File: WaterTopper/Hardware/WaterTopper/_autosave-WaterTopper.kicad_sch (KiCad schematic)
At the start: 61 parts, among them J1 TYPE-C-31-M-12, J2 Barrel_Jack_Switch, J3 Conn_01x07, J4 Conn_01x04, J5 Conn_01x04, J6 Conn_01x04, J7 Conn_01x04, J8 Screw_Terminal_01x02, J9 Screw_Terminal_01x02, SW1 SW_SPST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

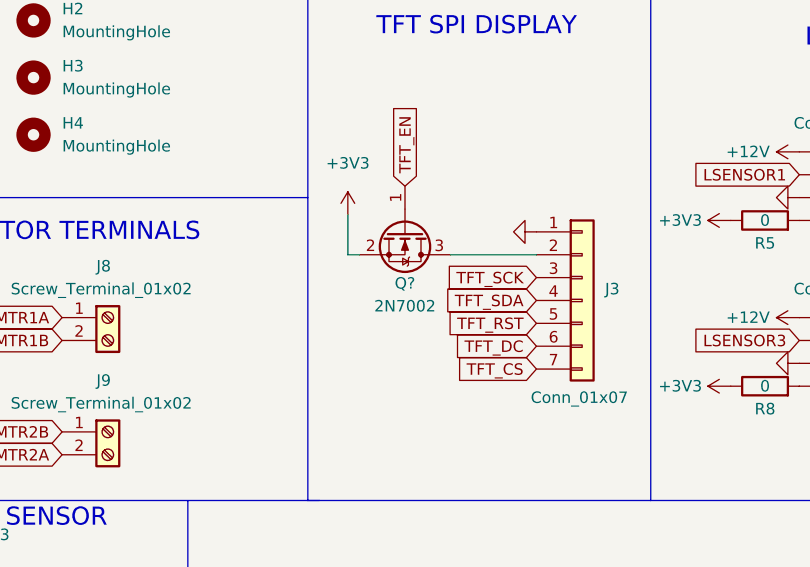
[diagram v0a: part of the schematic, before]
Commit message: Added small fixes + transistor for display
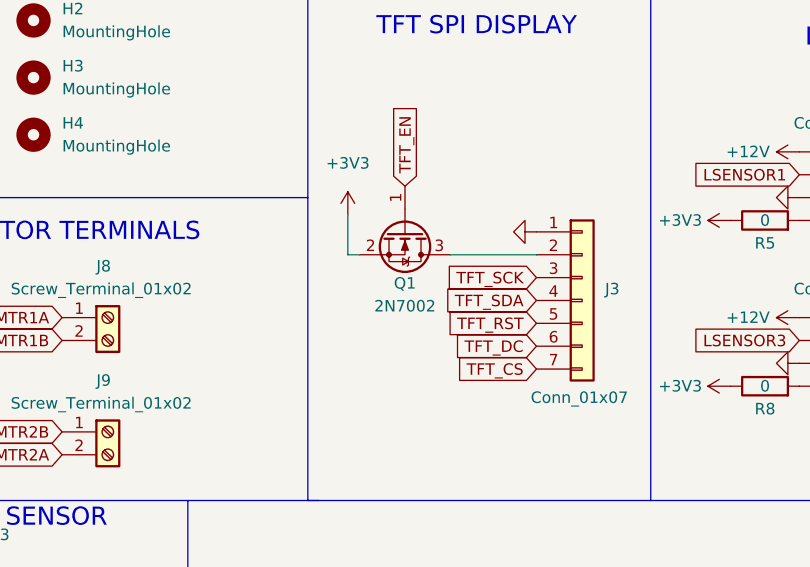
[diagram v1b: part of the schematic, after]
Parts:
- gave numbers to parts that had none: 1
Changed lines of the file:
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@@
   (symbol (lib_id "Transistor_FET:2N7002") (at 201.295 135.89 270) (unit 1)
     (in_bom yes) (on_board yes)
-    (property "Reference" "Q?" (id 0) (at 201.295 141.605 90))
+    (property "Reference" "Q1" (id 0) (at 201.295 141.605 90))
     (property "Value" "2N7002" (id 1) (at 201.295 144.145 90))
     (property "Footprint" "Package_TO_SOT_SMD:SOT-23" (id 2) (at 199.39 140.97 0)
@@
   (symbol (lib_id "power:+3V3") (at 194.945 133.985 0) (unit 1)
     (in_bom yes) (on_board yes) (fields_autoplaced)
-    (property "Reference" "#PWR?" (id 0) (at 194.945 137.795 0)
+    (property "Reference" "#PWR0126" (id 0) (at 194.945 137.795 0)
       (effects (font (size 1.27 1.27)) hide)
     )
@@
     )
     (path "/92e321f0-f634-47b7-9beb-7e112831b3a4"
-      (reference "#PWR?") (unit 1) (value "+3V3") (footprint "")
+      (reference "#PWR0126") (unit 1) (value "+3V3") (footprint "")
     )
     (path "/cd1fb780-87ab-4d7a-9da8-17057f510eeb"
@@
     )
     (path "/5a27f369-a855-44cd-b612-0fe1bf1ef58f"
-      (reference "Q?") (unit 1) (value "2N7002") (footprint "Package_TO_SOT_SMD:SOT-23")
+      (reference "Q1") (unit 1) (value "2N7002") (footprint "Package_TO_SOT_SMD:SOT-23")
     )
     (path "/60c0db67-3113-4bbf-832e-21f16f3c7d44"
